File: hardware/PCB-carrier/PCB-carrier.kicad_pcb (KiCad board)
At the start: 4 copper layers, 24 x 115.7 mm, 21 parts

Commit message: feat(carrier): drive the PS1240 from two pins in opposite phase -- cam D0 and D2
Operator, 2026-10-17: make the buzzer louder. TP_BUZ_G moves from GND to a new
net, BUZZER_B, on XIAO-ESP32S3-cam D2 (GPIO3); driven in opposite phase to D0
it doubles the swing across the disc, about +6 dB. D2 is quiet at boot; D6
would chirp the buzzer with the ROM's boot log. No hole moves.

verify_pins passes; 78 holes clear; DRC 0 violations, 15 unconnected (the new
net needs a trace now that the pad is off the GND plane). Docs: README nets,
PCB-carrier.md, the buzzer page, BOM, design.md; the template's callout.

Refs #25, #36

Co-Authored-By: Claude Opus 5.5 <noreply@anthropic.com>
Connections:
- J_CAM_A pad 3: (no net) -> BUZZER_B
- TP_BUZ_G pad 1: GND -> BUZZER_B

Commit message: fix(carrier): plain M3 holes for the female-female standoffs -- the board matches the fit mock
Operator, 2026-10-17: the PCB must match the fitted mock. The board still
carried Würth WA-SMSI surface-mount standoffs, chosen on paper in September and
never bought; the mock was mounted on female-female M3 hex standoffs with a
screw from each side. The two standoff footprints are now MountingHole_3.2mm_M3,
same positions; nothing to solder. The DRC exception for the Würth land pattern
is gone. The PS1240 stays at nose z 128.4: it fits beside standoff 2's screw
head on the printed mock (operator).

verify_pins and verify_clearances pass; DRC 0 violations, 15 unconnected
(unrouted). Fit mock regenerated (standoff holes now M3) and re-sliced: all 84
holes open in the G-code; plate in js-rocket ready/.

Refs #36, #16

Co-Authored-By: Claude Opus 5.5 <noreply@anthropic.com>
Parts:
- SO1, SO2: value Mounting_Wuerth_WA-SMSI-M3_H10mm_9774100360 -> MountingHole_3.2mm_M3; footprint Mounting_Wuerth_WA-SMSI-M3_H10mm_9774100360 -> MountingHole_3.2mm_M3; moved to F.Cu
- turned SO1 to 0 degrees
- turned SO2 to 0 degrees

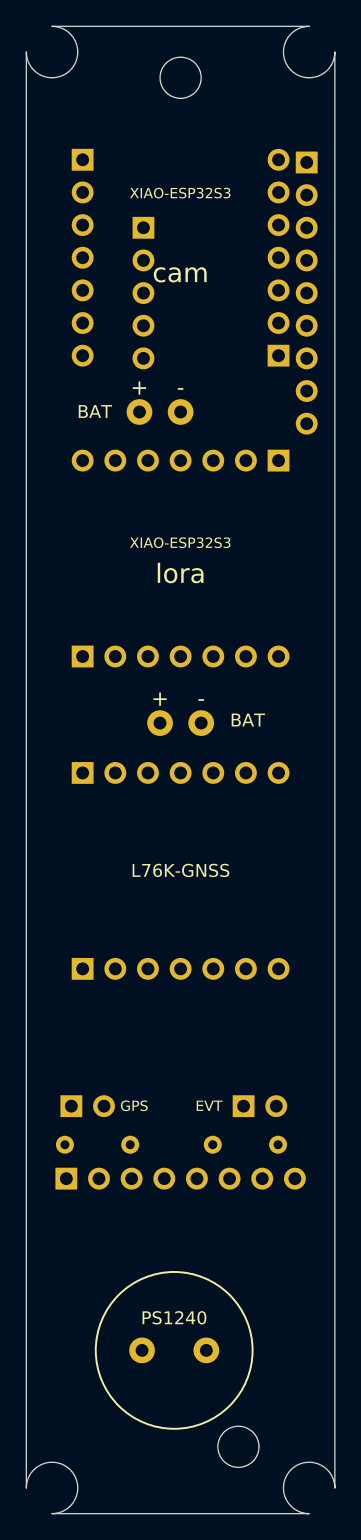
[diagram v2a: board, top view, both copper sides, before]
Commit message: feat(carrier): route the signal nets in the generator; fix the outline's corner arcs
#15. carrier_router.py is a grid A* router over F.Cu and B.Cu (0.127 mm grid,
0.25 mm track, 0.2 mm clearance, 0.6/0.3 mm vias), called by gen_carrier.py
after its pin and clearance checks. It routes the 12 signal nets -- I2C, GPS,
the GPS's own 3V3, the buzzer's two drive lines, the three data-link wires --
in 268 segments and 6 vias. Ground and +3V3 reach every pad through the inner
planes. KiCad DRC: 0 violations, 0 unconnected.

Also found while checking the routed board: all four corner arcs of the outline
swept 270 deg, not 90 -- a loop at each corner, there since the outline was
first written, which DRC passed and a board house could cut as drawn. Start
and end swapped; the generator now asserts 90 deg. The fit mock's corners
change with it (+0.08 cm3 back), so the mock is regenerated and re-sliced: all
84 holes open in the G-code, every corner solid. Reprint it.

Refs #15, #16

Co-Authored-By: Claude Opus 5.5 <noreply@anthropic.com>
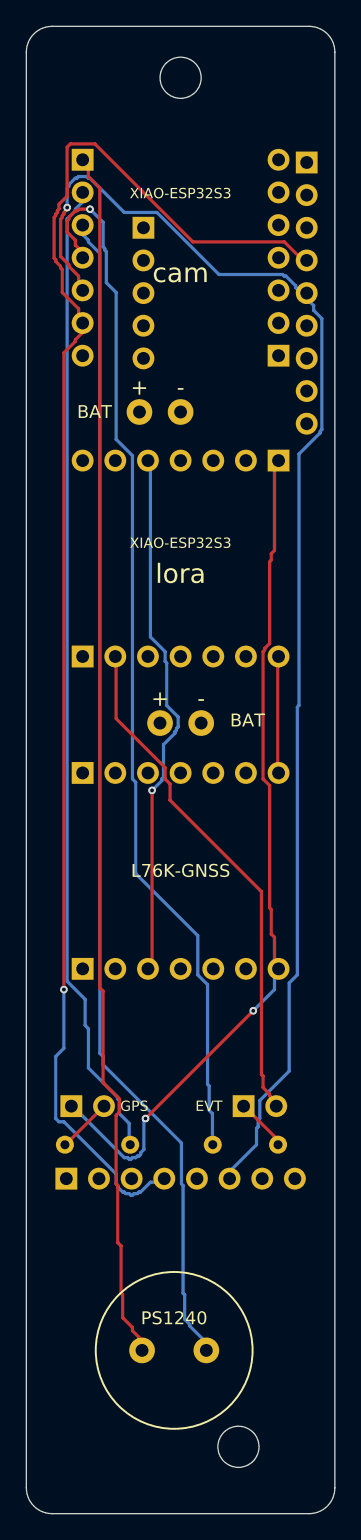
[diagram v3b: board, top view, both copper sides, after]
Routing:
- net SCL: track 0.00 -> 112.0 mm, vias 0 -> 1
- net SDA: track 0.00 -> 103.9 mm, vias 0 -> 1
- net BUZZER: track 0.00 -> 94.6 mm
- net BUZZER_B: track 0.00 -> 91.4 mm
- net EVT_CAM: track 0.00 -> 82.3 mm, vias 0 -> 1
- net GPS_CAM: track 0.00 -> 76.6 mm
- net GPS_RX: track 0.00 -> 66.5 mm, vias 0 -> 2
- net +3V3_LORA: track 0.00 -> 41.4 mm, vias 0 -> 1
- net EVT_LORA: track 0.00 -> 40.1 mm
- net GPS_TX: track 0.00 -> 9.07 mm
- net LINK_GPS: track 0.00 -> 4.27 mm
- net LINK_EVT: track 0.00 -> 4.08 mm
